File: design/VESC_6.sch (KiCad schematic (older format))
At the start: 23 parts, among them P1 USB_OTG, P2 CAN, P4 HALL_ENC, P5 COM, P6 SERVO, P7 SWD, U11 SENSOR_VOLTAGE

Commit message: Add ICM-20948 support
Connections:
- net labels added: +1V8
- wire segments 133 -> 134
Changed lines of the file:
@@
 S 1425 4075 650  325
 U 5A8CB300
-F0 "MPU9250" 60
-F1 "mpu9250.sch" 60
+F0 "ICM20948" 60
+F1 "icm20948.sch" 60
 F2 "SCL" I R 2075 4175 60
 F3 "SDA" I R 2075 4275 60
@@
 L power:PWR_FLAG #FLG020
 U 1 1 5A923350
-P 1775 6775
-F 0 "#FLG020" H 1775 6850 50  0001 C CNN
-F 1 "PWR_FLAG" V 1775 7125 50  0000 C CNN
-F 2 "" H 1775 6775 50  0001 C CNN
-F 3 "" H 1775 6775 50  0001 C CNN
-	1    1775 6775
-	0    -1   1    0
-$EndComp
-$Comp
-L power:PWR_FLAG #FLG021
-U 1 1 5A923358
 P 1775 6975
-F 0 "#FLG021" H 1775 7050 50  0001 C CNN
+F 0 "#FLG020" H 1775 7050 50  0001 C CNN
 F 1 "PWR_FLAG" V 1775 7325 50  0000 C CNN
 F 2 "" H 1775 6975 50  0001 C CNN
 F 3 "" H 1775 6975 50  0001 C CNN
 	1    1775 6975
+	0    -1   1    0
+$EndComp
+$Comp
+L power:PWR_FLAG #FLG021
+U 1 1 5A923358
+P 1775 7175
+F 0 "#FLG021" H 1775 7250 50  0001 C CNN
+F 1 "PWR_FLAG" V 1775 7525 50  0000 C CNN
+F 2 "" H 1775 7175 50  0001 C CNN
+F 3 "" H 1775 7175 50  0001 C CNN
+	1    1775 7175
 	0    -1   1    0
 $EndComp
@@
 $EndComp
 $Comp
-L power:VCC #PWR023
+L power:VCC #PWR024
 U 1 1 5A923BEC
-P 2350 6775
-F 0 "#PWR023" H 2350 6625 50  0001 C CNN
-F 1 "VCC" V 2350 6975 50  0000 C CNN
-F 2 "" H 2350 6775 50  0001 C CNN
-F 3 "" H 2350 6775 50  0001 C CNN
-	1    2350 6775
-	0    1    1    0
-$EndComp
-$Comp
-L power:GND #PWR024
+P 2350 6975
+F 0 "#PWR024" H 2350 6825 50  0001 C CNN
+F 1 "VCC" V 2350 7175 50  0000 C CNN
+F 2 "" H 2350 6975 50  0001 C CNN
+F 3 "" H 2350 6975 50  0001 C CNN
+	1    2350 6975
+	0    1    1    0
+$EndComp
+$Comp
+L power:GND #PWR025
 U 1 1 5A923F94
-P 2375 6975
-F 0 "#PWR024" H 2375 6725 50  0001 C CNN
-F 1 "GND" V 2375 6775 50  0000 C CNN
-F 2 "" H 2375 6975 50  0001 C CNN
-F 3 "" H 2375 6975 50  0001 C CNN
-	1    2375 6975
+P 2375 7175
+F 0 "#PWR025" H 2375 6925 50  0001 C CNN
+F 1 "GND" V 2375 6975 50  0000 C CNN
+F 2 "" H 2375 7175 50  0001 C CNN
+F 3 "" H 2375 7175 50  0001 C CNN
+	1    2375 7175
 	0    -1   -1   0
 $EndComp
 $Comp
-L power:VCC #PWR025
+L power:VCC #PWR0101
 U 1 1 5A960E55
 P 1875 1775
-F 0 "#PWR025" H 1875 1625 50  0001 C CNN
+F 0 "#PWR0101" H 1875 1625 50  0001 C CNN
 F 1 "VCC" H 1875 1925 50  0000 C CNN
 F 2 "" H 1875 1775 50  0001 C CNN
@@
 	8300 4100 8075 4100
 Wire Wire Line
-	1775 6975 2375 6975
-Wire Wire Line
-	1775 6775 2350 6775
+	1775 7175 2375 7175
+Wire Wire Line
+	1775 6975 2350 6975
 Wire Wire Line
 	1775 6575 2350 6575
@@
 NoConn ~ 3050 1350
 NoConn ~ 8300 4600
+$Comp
+L power:PWR_FLAG #FLG0101
+U 1 1 5DD25A4E
+P 1775 6775
+F 0 "#FLG0101" H 1775 6850 50  0001 C CNN
+F 1 "PWR_FLAG" V 1775 7125 50  0000 C CNN
+F 2 "" H 1775 6775 50  0001 C CNN
+F 3 "" H 1775 6775 50  0001 C CNN
+	1    1775 6775
+	0    -1   1    0
+$EndComp
+Wire Wire Line
+	1775 6775 2350 6775
+$Comp
+L power:+1V8 #PWR023
+U 1 1 5DD25A54
+P 2350 6775
+F 0 "#PWR023" H 2350 6625 50  0001 C CNN
+F 1 "+1V8" V 2350 7000 50  0000 C CNN
+F 2 "" H 2350 6775 50  0001 C CNN
+F 3 "" H 2350 6775 50  0001 C CNN
+	1    2350 6775
+	0    1    1    0
+$EndComp
 $EndSCHEMATC

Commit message: Revert "Add ICM-20948 support"
This reverts commit 6973a9f76e2e1207f1c7879789cf7605503054ef.
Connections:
- net labels removed: +1V8
- wire segments 134 -> 133
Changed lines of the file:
@@
 S 1425 4075 650  325
 U 5A8CB300
-F0 "ICM20948" 60
-F1 "icm20948.sch" 60
+F0 "MPU9250" 60
+F1 "mpu9250.sch" 60
 F2 "SCL" I R 2075 4175 60
 F3 "SDA" I R 2075 4275 60
@@
 L power:PWR_FLAG #FLG020
 U 1 1 5A923350
+P 1775 6775
+F 0 "#FLG020" H 1775 6850 50  0001 C CNN
+F 1 "PWR_FLAG" V 1775 7125 50  0000 C CNN
+F 2 "" H 1775 6775 50  0001 C CNN
+F 3 "" H 1775 6775 50  0001 C CNN
+	1    1775 6775
+	0    -1   1    0
+$EndComp
+$Comp
+L power:PWR_FLAG #FLG021
+U 1 1 5A923358
 P 1775 6975
-F 0 "#FLG020" H 1775 7050 50  0001 C CNN
+F 0 "#FLG021" H 1775 7050 50  0001 C CNN
 F 1 "PWR_FLAG" V 1775 7325 50  0000 C CNN
 F 2 "" H 1775 6975 50  0001 C CNN
 F 3 "" H 1775 6975 50  0001 C CNN
 	1    1775 6975
-	0    -1   1    0
-$EndComp
-$Comp
-L power:PWR_FLAG #FLG021
-U 1 1 5A923358
-P 1775 7175
-F 0 "#FLG021" H 1775 7250 50  0001 C CNN
-F 1 "PWR_FLAG" V 1775 7525 50  0000 C CNN
-F 2 "" H 1775 7175 50  0001 C CNN
-F 3 "" H 1775 7175 50  0001 C CNN
-	1    1775 7175
 	0    -1   1    0
 $EndComp
@@
 $EndComp
 $Comp
-L power:VCC #PWR024
+L power:VCC #PWR023
 U 1 1 5A923BEC
-P 2350 6975
-F 0 "#PWR024" H 2350 6825 50  0001 C CNN
-F 1 "VCC" V 2350 7175 50  0000 C CNN
-F 2 "" H 2350 6975 50  0001 C CNN
-F 3 "" H 2350 6975 50  0001 C CNN
-	1    2350 6975
-	0    1    1    0
-$EndComp
-$Comp
-L power:GND #PWR025
+P 2350 6775
+F 0 "#PWR023" H 2350 6625 50  0001 C CNN
+F 1 "VCC" V 2350 6975 50  0000 C CNN
+F 2 "" H 2350 6775 50  0001 C CNN
+F 3 "" H 2350 6775 50  0001 C CNN
+	1    2350 6775
+	0    1    1    0
+$EndComp
+$Comp
+L power:GND #PWR024
 U 1 1 5A923F94
-P 2375 7175
-F 0 "#PWR025" H 2375 6925 50  0001 C CNN
-F 1 "GND" V 2375 6975 50  0000 C CNN
-F 2 "" H 2375 7175 50  0001 C CNN
-F 3 "" H 2375 7175 50  0001 C CNN
-	1    2375 7175
+P 2375 6975
+F 0 "#PWR024" H 2375 6725 50  0001 C CNN
+F 1 "GND" V 2375 6775 50  0000 C CNN
+F 2 "" H 2375 6975 50  0001 C CNN
+F 3 "" H 2375 6975 50  0001 C CNN
+	1    2375 6975
 	0    -1   -1   0
 $EndComp
 $Comp
-L power:VCC #PWR0101
+L power:VCC #PWR025
 U 1 1 5A960E55
 P 1875 1775
-F 0 "#PWR0101" H 1875 1625 50  0001 C CNN
+F 0 "#PWR025" H 1875 1625 50  0001 C CNN
 F 1 "VCC" H 1875 1925 50  0000 C CNN
 F 2 "" H 1875 1775 50  0001 C CNN
@@
 	8300 4100 8075 4100
 Wire Wire Line
-	1775 7175 2375 7175
-Wire Wire Line
-	1775 6975 2350 6975
+	1775 6975 2375 6975
+Wire Wire Line
+	1775 6775 2350 6775
 Wire Wire Line
 	1775 6575 2350 6575
@@
 NoConn ~ 3050 1350
 NoConn ~ 8300 4600
-$Comp
-L power:PWR_FLAG #FLG0101
-U 1 1 5DD25A4E
-P 1775 6775
-F 0 "#FLG0101" H 1775 6850 50  0001 C CNN
-F 1 "PWR_FLAG" V 1775 7125 50  0000 C CNN
-F 2 "" H 1775 6775 50  0001 C CNN
-F 3 "" H 1775 6775 50  0001 C CNN
-	1    1775 6775
-	0    -1   1    0
-$EndComp
-Wire Wire Line
-	1775 6775 2350 6775
-$Comp
-L power:+1V8 #PWR023
-U 1 1 5DD25A54
-P 2350 6775
-F 0 "#PWR023" H 2350 6625 50  0001 C CNN
-F 1 "+1V8" V 2350 7000 50  0000 C CNN
-F 2 "" H 2350 6775 50  0001 C CNN
-F 3 "" H 2350 6775 50  0001 C CNN
-	1    2350 6775
-	0    1    1    0
-$EndComp
 $EndSCHEMATC

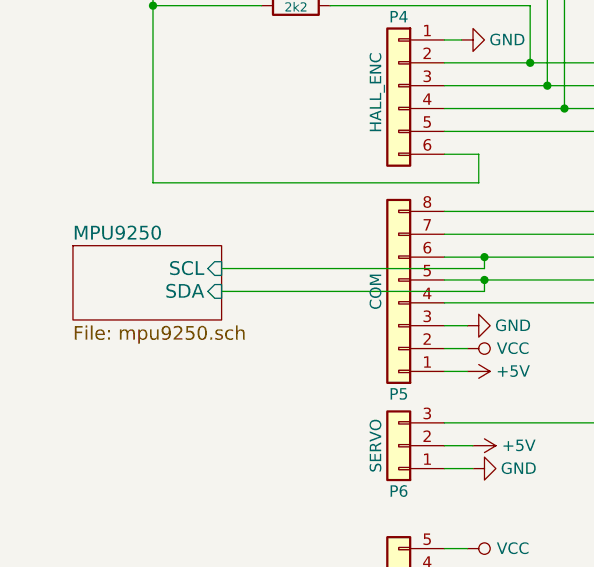
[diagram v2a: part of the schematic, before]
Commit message: Enable MPU-9150
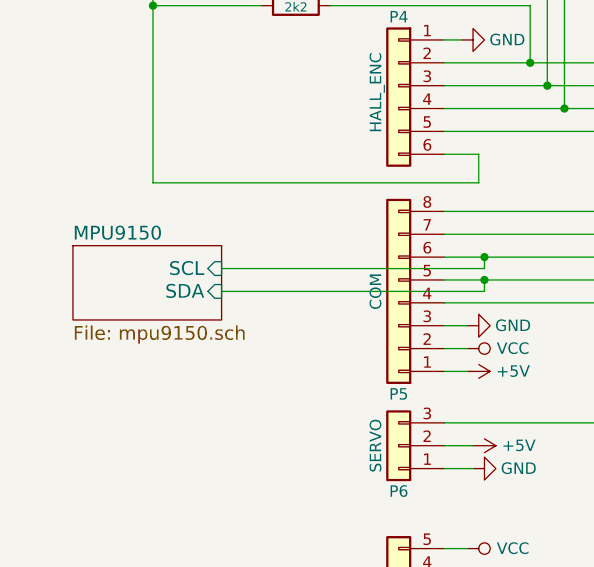
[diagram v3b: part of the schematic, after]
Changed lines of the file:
@@
 S 1425 4075 650  325
 U 5A8CB300
-F0 "MPU9250" 60
-F1 "mpu9250.sch" 60
+F0 "MPU9150" 60
+F1 "mpu9150.sch" 60
 F2 "SCL" I R 2075 4175 60
 F3 "SDA" I R 2075 4275 60
